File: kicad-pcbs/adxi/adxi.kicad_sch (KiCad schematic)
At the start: 139 parts, among them J3 USBC, J5 USB2 Type-A, J7 12-24V SUPPLY, Q1 MMBF170, Q2 HY1904C2, U1 SI5351A-B-GTR, U10 CM108B, U2 CD2003, U3 L7812, U4 74ACT244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

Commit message: Improvements to receiver
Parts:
- removed C14: 620pF, symbol Device:C_Small
- removed C56: 100nF, symbol Device:C_Small
- removed C57: 10nF, symbol Device:C_Small
- added C37: 10nF, Capacitor_SMD:C_0603_1608Metric, symbol Device:C_Small
- added C38: 100nF, Capacitor_SMD:C_0805_2012Metric, symbol Device:C_Small
- added C39, C40: 220pF, Capacitor_SMD:C_0603_1608Metric, symbol Device:C_Small
- added R24, R25: 10K, Resistor_SMD:R_0402_1005Metric, symbol Device:R_Small_US
- C10, C13, C32, C7, C9: footprint (none) -> Capacitor_SMD:C_0805_2012Metric; LCSC Part # (none) -> C28233; MPN (none) -> CL21B104KCFNNNE; Manfacturer (none) -> Samsung
- C11: value C_Small -> 220pF; footprint (none) -> Capacitor_SMD:C_0603_1608Metric; LCSC Part # (none) -> C1603; MPN (none) -> CL10B221KB8NNNC; Manufacturer (none) -> Samsung
- C12: footprint (none) -> Capacitor_SMD:C_1206_3216Metric; symbol Device:C_Polarized_Small -> Device:C_Small; LCSC Part # (none) -> C15008; MPN (none) -> CL31A107MQHNNNE; Manufacturer (none) -> Samsung
- C17, C19, C28: footprint (none) -> Capacitor_SMD:C_0603_1608Metric; LCSC Part # (none) -> C57112; MPN (none) -> 0603B103K500NT; Manufacturer (none) -> Fenghua
- C26, C55: footprint (none) -> Capacitor_SMD:C_0603_1608Metric; LCSC Part # (none) -> C15849; MPN (none) -> CL10A105KB8NNNC; Manufacturer (none) -> Samsung
- C27: footprint (none) -> Capacitor_SMD:C_0603_1608Metric; LCSC Part # (none) -> C14663; MPN (none) -> CC0603KRX7R9BB104; Manufacturer (none) -> Yageo
- L1, L2: Notes For 40M band, 7-7.3MHz -> (none)
- U2: footprint Package_SO:SOP-16_4.55x10.3mm_P1.27mm -> Package_SO:SOP-16_3.9x9.9mm_P1.27mm; LCSC Part # (none) -> C7421626
- U3: footprint (none) -> Package_TO_SOT_SMD:TO-263-2; LCSC Part # (none) -> C22357877; MPN (none) -> L7812CDTR(XBLW); Manufacturer (none) -> XBLW
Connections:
- net 3.3V: now also C9.2, R24.1, R25.1; no longer C9.1
- net 5V: now also C28.2, C37.2, C38.2; no longer C28.1
- net GND: now also C28.1, C9.1, C37.1, C38.1; no longer C28.2, C9.2
- net I2C-SCL-3.3V: now also R25.2
- net I2C-SDA-3.3V: now also R24.2
- net at Q2.4 (GATE), R15.2: now also C32.1; no longer C32.2
- net at Q1.3 (D), R14.1: now also C11.2, C39.2, C40.2
- net at D5.2 (A), D6.1 (K), L1.2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: now also C11.1, C39.1, C40.1; no longer C11.2
- net at C10.2, C21.2, C22.2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: no longer C11.1
- net at U4.12 (1Y3), U4.14 (1Y2), U4.16 (1Y1)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: now also C32.2; no longer C32.1
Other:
- note added: "(3 x 220pF = 660pF)"
- note added: "AM ONLY"
- note added: "I2C 3.3V BUS PULLUPS"
- note added: "NO FM"
- note added: "SEE doc/filter-models/cd2003-rf-low-pass-filter"
- note added: "SIGNAL CLAMP"
- note added: "THE CD2003 IS A CLONE OF THE TA2003, ITSELF PIN-COMPATIBLE TO THE OLDER TA8164. ONLY THE AM SECTION IS USED AS A DIRECT CONVERSION RECEIVER."
- note removed: "CD2003GP IS A CLONE OF TA2003, ITSELF A PIN-COMPATIBLE UPGRADE TO TA8164. ONLY THE AM SECTION IS USED AS A DIRECT CONVERSION RECEIVER."
- moved on the sheet: C15, C16, C17, C21, C22, C24, D5, D6, L1, L2, L3, Q1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

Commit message: More work, getting close now!
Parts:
- removed C12: 100uF, Capacitor_SMD:C_1206_3216Metric, symbol Device:C_Small
- removed C22: 10uF, Capacitor_SMD:C_1206_3216Metric, symbol Device:C_Small
- removed L3: 100uH, Inductor_SMD:L_TaiTech_TMPC1265_13.5x12.5mm, symbol Device:L
- removed R101, R102: 1K, Resistor_SMD:R_0603_1608Metric, symbol Device:R_Small_US
- added C12, C14: 470uF, Capacitor_SMD:C_Elec_10x10.2, symbol Device:C_Polarized_Small
- added C2, C4, C6: 100nF, Capacitor_SMD:C_0603_1608Metric, symbol Device:C_Small
- added C3: 10uF, Capacitor_SMD:C_0603_1608Metric, symbol Device:C_Small
- added R26: 10, Resistor_SMD:R_1206_3216Metric, symbol Device:R_Small_US
- added R27, R28, R29: 22K, Resistor_SMD:R_0805_2012Metric, symbol Device:R_Small_US
- added R30: 100, Resistor_SMD:R_0805_2012Metric, symbol Device:R_Small_US
- added U6: LMV358CDRG, adxi-footprints:SOIC-8_L4.9-W3.9-P1.27-LS6.0-TL, symbol adxi-symbols:LMV358CDRG
- C21: value 100nF -> 10uF; footprint Capacitor_SMD:C_0805_2012Metric -> Capacitor_SMD:C_1206_3216Metric; LCSC Part # C28233 -> C13585; MPN CL21B104KCFNNNE -> CL31A106KBHNNNE; Manfacturer Samsung -> (none); Manufacturer (none) -> Samsung
- J7: footprint Connector_BarrelJack:BarrelJack_GCT_DCJ200-10-A_Horizontal -> adxi-footprints:DC-IN-TH_DC550250-0366-2H
- L4: footprint Inductor_SMD:L_TaiTech_TMPC1265_13.5x12.5mm -> adxi-footprints:IND-SMD_L13.4-W12.6
- Q2: footprint kicad-parts:HY1904C2 -> kicad-6-parts:HY1904C2; MPN (none) -> HY1904C2; Manufacturer (none) -> Huayi
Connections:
- net PA-DRAIN is gone; now on net RECEIVED-SIGNAL: D11.2 (A), Q2.5 (DRAIN_5), Q2.6 (DRAIN_6), Q2.7 (DRAIN_7), Q2.8 (DRAIN_8), R1.2, R9.2, TP13.1
- net 5V: now also C2.1, C3.1, R26.1, U6.8 (VDD); no longer C16.2
- net GND: now also C12.2, C14.2, C2.2, C3.2, U6.4 (VSS), U6.5 (INB+), U6.6 (INB-)
- net HOST-FSK-INPUT: now also R30.2
- net at U10.30 (LOL): now also C4.1
- net at C10.2, C21.2, C24.2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: now also C16.2, C12.1, C14.1, R26.2
- net at U10.32 (LOR): now also C6.1
- net HOST-FSK-BIAS renamed 1.75V-BIAS
- net 1.75V-BIAS: now also U6.3 (INA+)
- net IFAULT-WHEN-LOW: no longer names the net of U7.6 (~{VCONN_FAULT})
- net PDSW renamed SLEEP-WHEN-LOW
- net VOLDN renamed VOLUME-DOWN-BUTTON-WHEN-LOW
- new net: R27.2, R28.2, R29.1, U6.2 (INA-)
- new net: R29.2, R30.1, U6.1 (OUTA)
- new net: C6.2, R28.1
- new net: C4.2, R27.1
- no-connect marks 57 -> 59
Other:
- removed sheet pa-lpf-ant
- sheet PA Transmit Power Modulation ports: added none; removed 5V
- note added: "LOW PASS 'RC' FILTER (LPF)"
- note added: "TO DEMODULATION AND FP/RP/SWR DETECTION"
- note removed: "ADD PULLUPS/PULLDOWNS ADD OPTIONAL SQUEAKER ADD TEST POINTS"
- note removed: "TO SWR DETECTION"
- moved on the sheet: C1, C37, C38, C46, C5, C53, C54, C55, D1, D2, D3, D4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

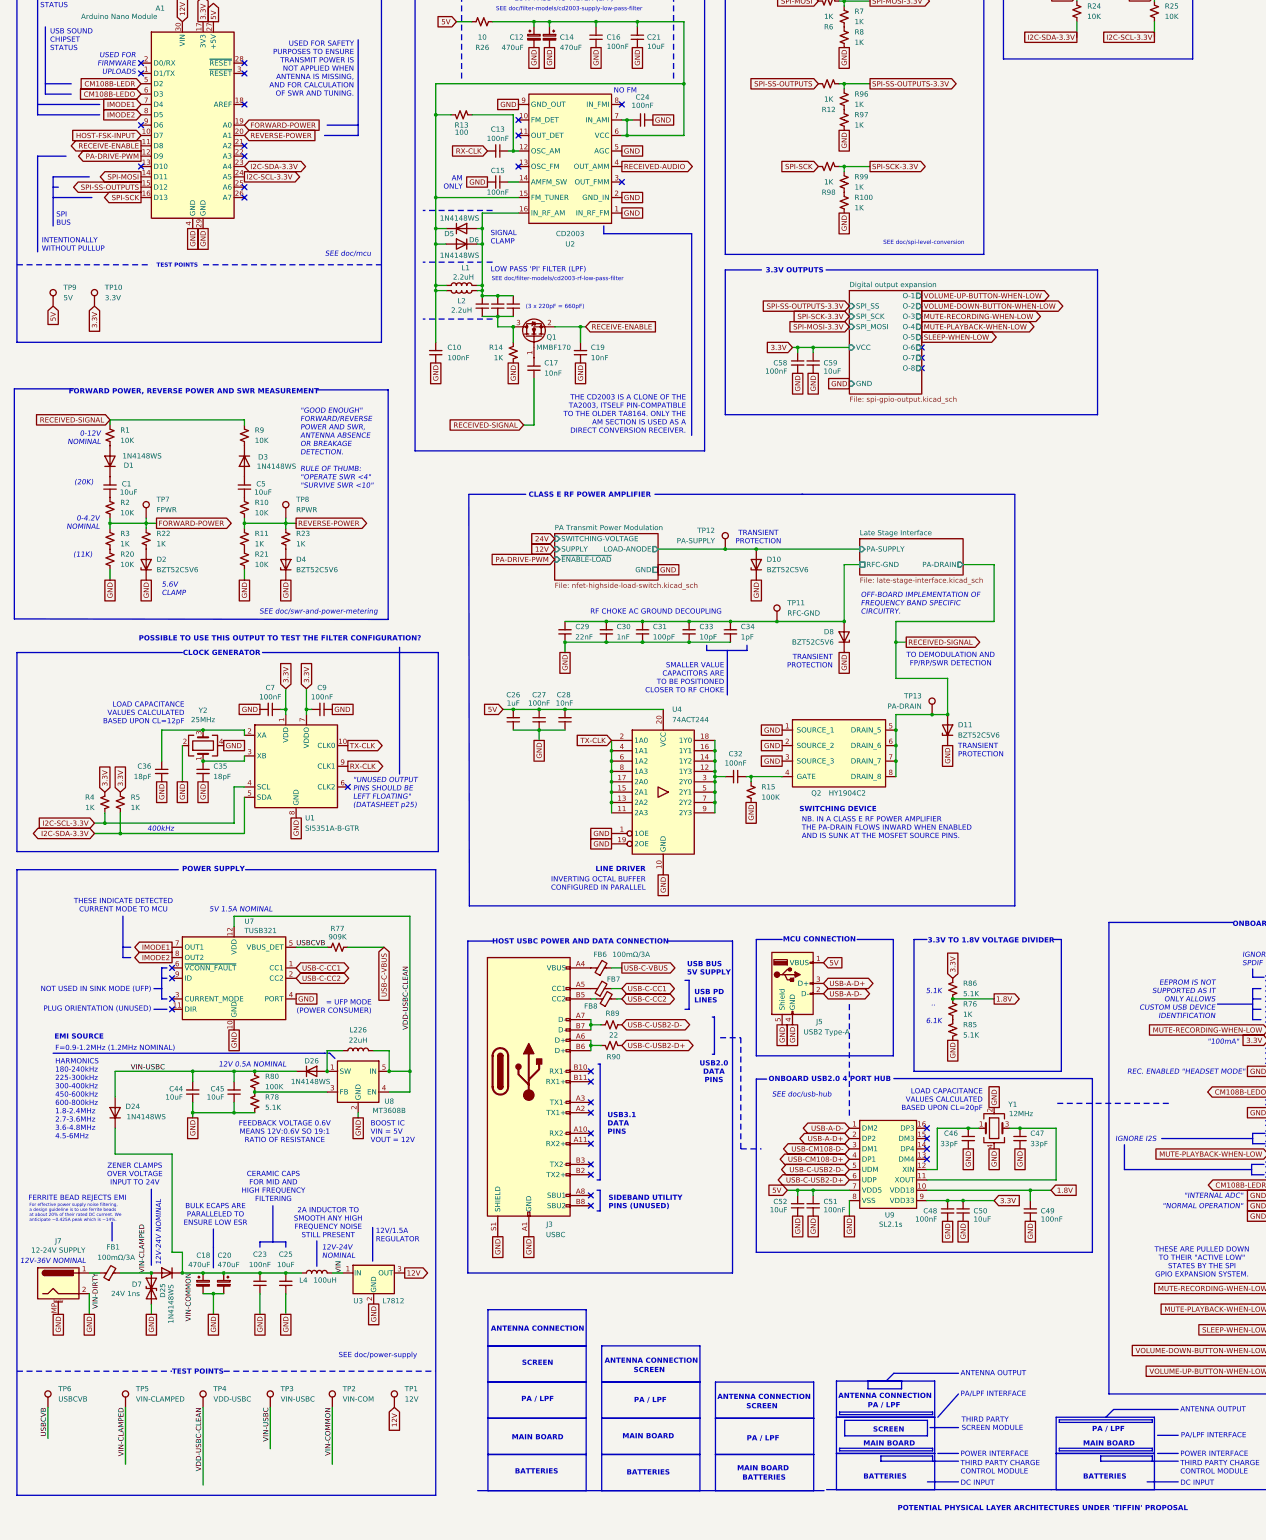
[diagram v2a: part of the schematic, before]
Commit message: Simplify PSU, add 4xM3 mounting holes, silkscreen, better footprints
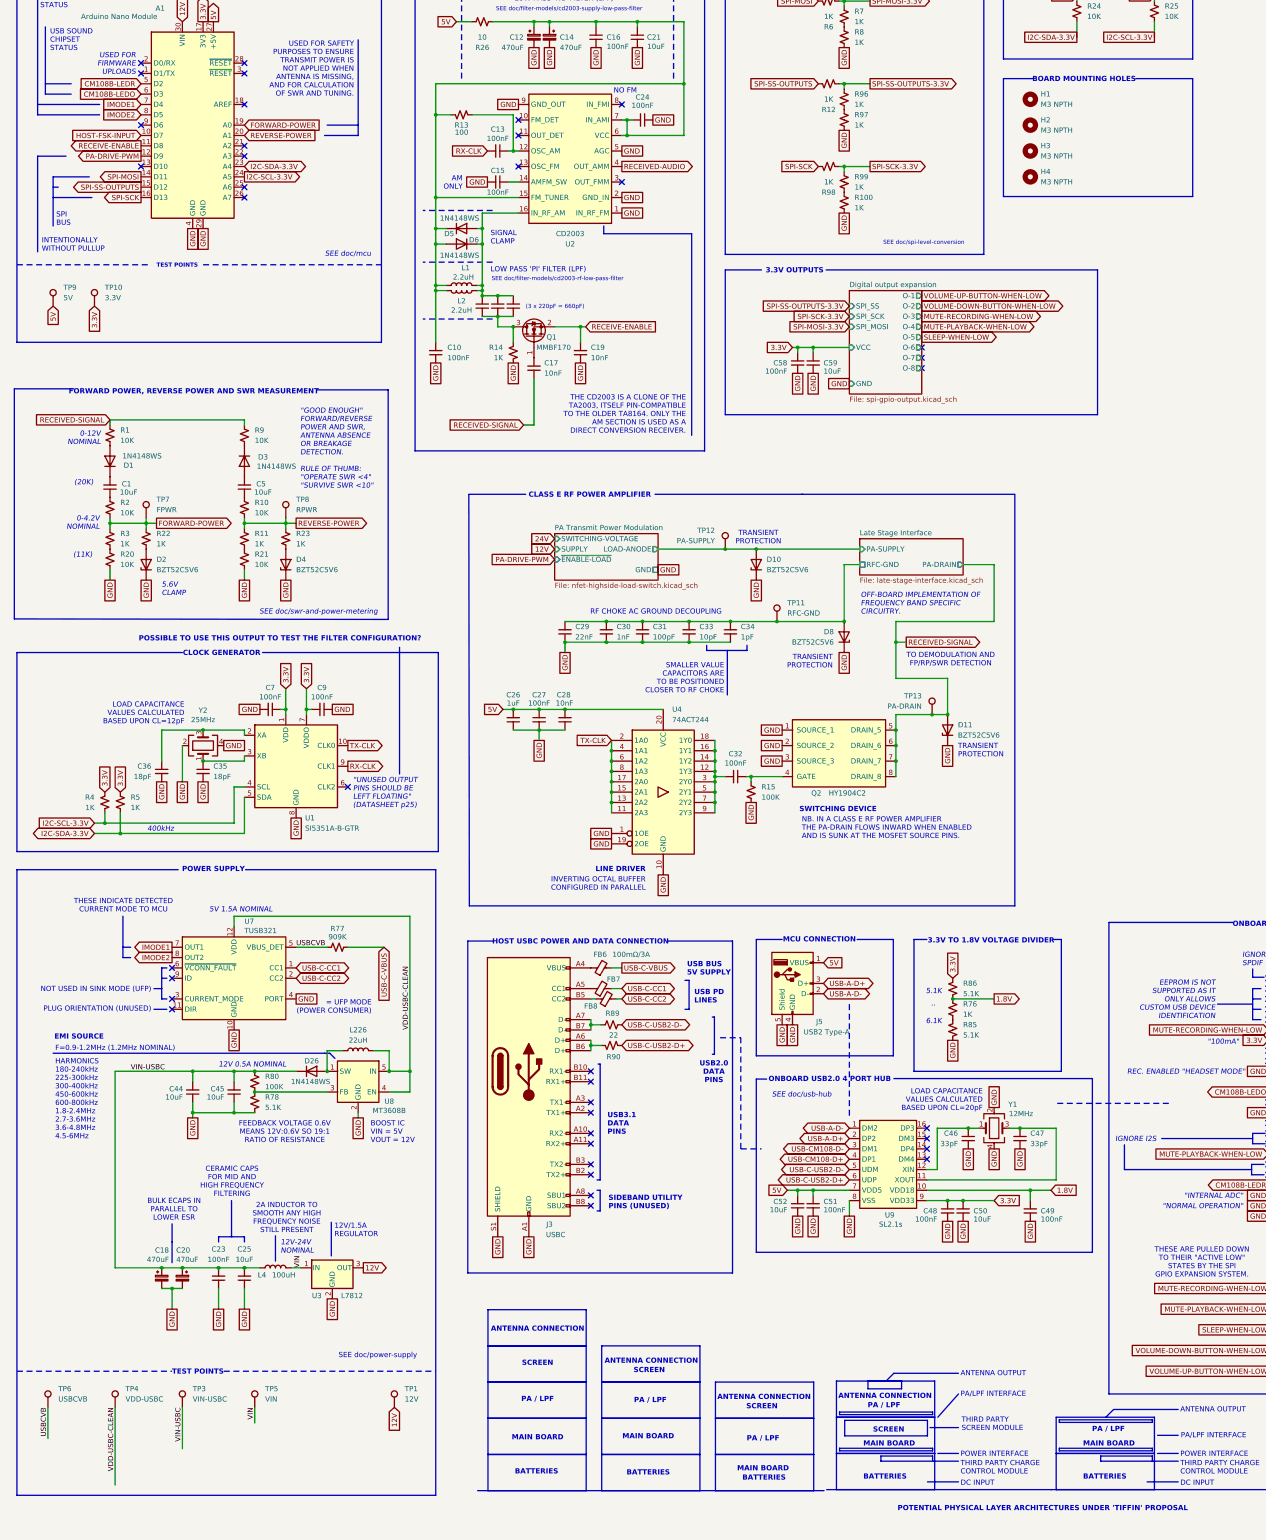
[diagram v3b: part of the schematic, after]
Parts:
- removed D24, D25: 1N4148WS, Diode_SMD:D_SOD-323, symbol Diode:1N4148WS
- removed D7: 24V 1ns, Diode_SMD:D_0603_1608Metric, symbol Diode:SD15_SOD323
- removed FB1: 100mΩ/3A, Capacitor_SMD:C_1206_3216Metric, symbol Device:FerriteBead_Small
- removed J7: 12-24V SUPPLY, adxi-footprints:DC-IN-TH_DC550250-0366-2H, symbol Connector:Barrel_Jack_MountingPin
- removed TP2: VIN-COM, TestPoint:TestPoint_Plated_Hole_D2.0mm, symbol Connector:TestPoint
- added H1, H2, H3, H4: M3 NPTH, MountingHole:MountingHole_3.2mm_M3_DIN965, symbol Mechanical:MountingHole
- Q2: footprint kicad-6-parts:HY1904C2 -> adxi-footprints:DFN-8_L5.9-W5.2-P1.27-LS6.2-BL
- TP5: value VIN-CLAMPED -> VIN
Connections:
- net VIN-CLAMPED is gone; now on net VIN: TP5.1
- net VIN-COMMON is gone; now on net VIN-USBC: C18.1, C20.1, C23.2, C25.2, L4.1
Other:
- note added: "BOARD MOUNTING HOLES"
- note added: "BULK ECAPS IN PARALLEL TO LOWER ESR"
- note removed: "12V-36V NOMINAL"
- note removed: "BULK ECAPS ARE PARALLELED TO ENSURE LOW ESR"
- note removed: "FERRITE BEAD REJECTS EMI"
- note removed: "For effective power supply noise filtering, a design guideline is to use ferrite beads at about 20% of their rated DC current. We anticipate ~0.425A peak which is ~14%."
- note removed: "ZENER CLAMPS OVER VOLTAGE INPUT TO 24V"
- moved on the sheet: C18, C20, C23, C25, L4, TP3, TP4, TP5, U3

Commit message: Layout complete
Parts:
- added C8: 470uF, Capacitor_SMD:C_Elec_10x10.2, symbol Device:C_Polarized_Small
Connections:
- net 12V: now also C8.1
- net GND: now also C8.2
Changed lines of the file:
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@@
 	)
 	(junction
+		(at 110.49 342.9)
+		(diameter 0)
+		(color 0 0 0 0)
+	)
+	(junction
 		(at 238.76 218.44)
 		(diameter 0)
@@
 	(wire
 		(pts
+			(xy 107.95 342.9) (xy 110.49 342.9)
+		)
+		(stroke
+			(width 0)
+			(type default)
+		)
+	)
+	(wire
+		(pts
 			(xy 427.99 271.78) (xy 427.99 293.37)
 		)
@@
 		)
 	)
+	(wire
+		(pts
+			(xy 110.49 342.9) (xy 115.57 342.9)
+		)
+		(stroke
+			(width 0)
+			(type default)
+		)
+	)
 	(polyline
 		(pts
@@
 	(global_label "12V"
 		(shape output)
-		(at 107.95 342.9 0)
+		(at 115.57 342.9 0)
 		(fields_autoplaced yes)
 		(effects
@@
 		)
 		(property "Intersheetrefs" "${INTERSHEET_REFS}"
-			(at 114.4428 342.9 0)
+			(at 122.0628 342.9 0)
 			(effects
 				(font
@@
 		)
 	)
+	(global_label "GND"
+		(shape passive)
+		(at 110.49 347.98 270)
+		(fields_autoplaced yes)
+		(effects
+			(font
+				(size 1.27 1.27)
+			)
+			(justify right)
+		)
+		(property "Intersheetrefs" "${INTERSHEET_REFS}"
+			(at 110.49 353.7244 90)
+			(effects
+				(font
+					(size 1.27 1.27)
+				)
+				(justify right)
+				(hide yes)
+			)
+		)
+	)
 	(global_label "12V"
 		(shape input)
@@
 					(unit 1)
 				)
+			)
+		)
+	)
+	(symbol
+		(lib_id "Device:C_Polarized_Small")
+		(at 110.49 345.44 0)
+		(mirror y)
+		(unit 1)
+		(exclude_from_sim no)
+		(in_bom yes)
+		(on_board yes)
+		(dnp no)
+		(property "Reference" "C8"
+			(at 108.966 338.582 0)
+			(effects
+				(font
+					(size 1.27 1.27)
+				)
+				(justify right)
+			)
+		)
+		(property "Value" "470uF"
+			(at 108.966 340.868 0)
+			(effects
+				(font
+					(size 1.27 1.27)
+				)
+				(justify right)
+			)
+		)
+		(property "Footprint" "Capacitor_SMD:C_Elec_10x10.2"
+			(at 110.49 345.44 0)
+			(effects
+				(font
+					(size 1.27 1.27)
+				)
+				(hide yes)
+			)
+		)
+		(property "Datasheet" "https://wmsc.lcsc.com/wmsc/upload/file/pdf/v2/lcsc/2202252130_ROQANG-RVE1E471M1010_C107397.pdf"
+			(at 110.49 345.44 0)
+			(effects
+				(font
+					(size 1.27 1.27)
+				)
+				(hide yes)
+			)
+		)
+		(property "Description" "Polarized capacitor, small symbol"
+			(at 110.49 345.44 0)
+			(effects
+				(font
+					(size 1.27 1.27)
+				)
+				(hide yes)
+			)
+		)
+		(property "LCSC Part #" "C107397"
+			(at 110.49 345.44 0)
+			(effects
+				(font
+					(size 1.27 1.27)
+				)
+				(hide yes)
+			)
+		)
+		(property "MPN" "RVE1E471M1010"
+			(at 110.49 345.44 0)
+			(effects
+				(font
+					(size 1.27 1.27)
+				)
+				(hide yes)
+			)
+		)
+		(property "Manufacturer" "Roqang"
+			(at 110.49 345.44 0)
+			(effects
+				(font
+					(size 1.27 1.27)
+				)
+				(hide yes)
+			)
+		)
+		(pin "1"
+		)
+		(pin "2"
+		)
+		(instances
+			(project "adxi"
+				(path "/c3abf330-1856-4368-a03b-0e6191ae29a9"
+					(reference "C8")
+					(unit 1)
+				)

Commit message: Fixed vias
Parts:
- added TP14, TP15, TP2: GND, TestPoint:TestPoint_THTPad_2.0x2.0mm_Drill1.0mm, symbol Connector:TestPoint
- TP1, TP10, TP11, TP12, TP13, TP3, TP4, TP5, TP6, TP7, TP8, TP9: footprint TestPoint:TestPoint_Plated_Hole_D2.0mm -> TestPoint:TestPoint_THTPad_2.0x2.0mm_Drill1.0mm
- U7: LCSC Part # (none) -> C139392; MPN (none) -> TUSB321RWBR; Manufacturer (none) -> TI
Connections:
- net GND: now also TP14.1, TP15.1, TP2.1
